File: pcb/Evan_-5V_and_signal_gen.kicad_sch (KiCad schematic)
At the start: 34 parts, among them IC1 TL7660IDGKR, IC2 TL081IDT, IC4 UA78M33CDCYG3, IC9 TL081IDT, J2 ESQ-126-39-L-D, J3 ESQ-126-39-L-D, U5 TPS2069CDBVR_MOSFET

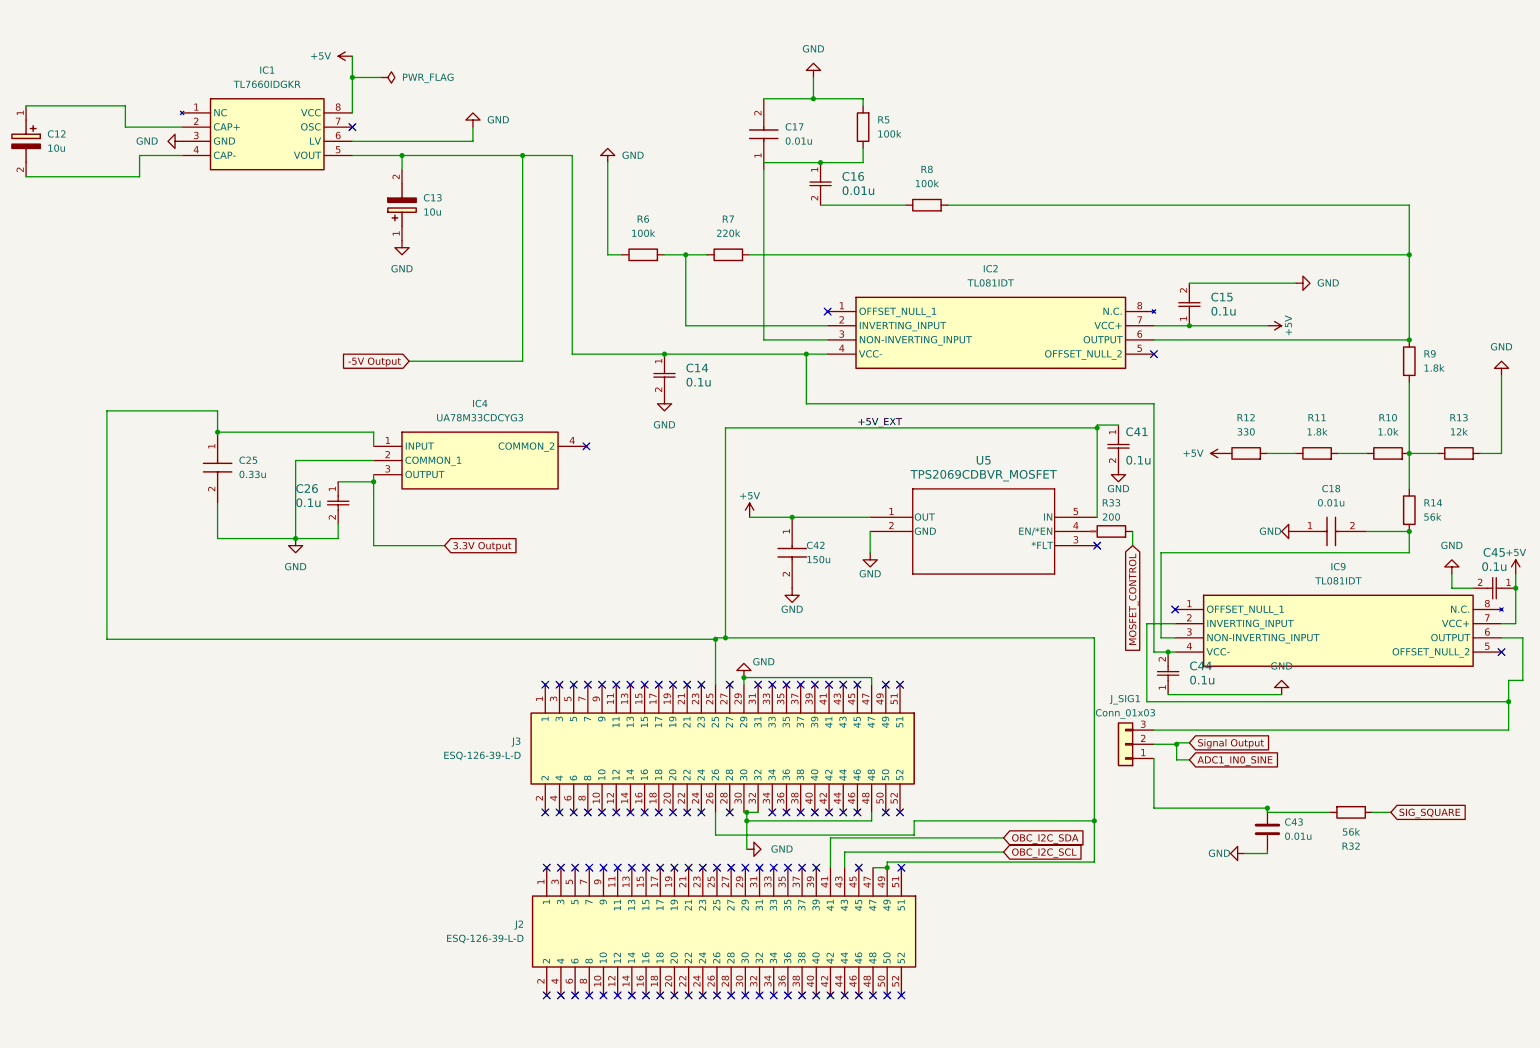
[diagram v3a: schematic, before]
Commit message: clean evan schematic (#22)
* clean evan schematic

* update schematic pdf
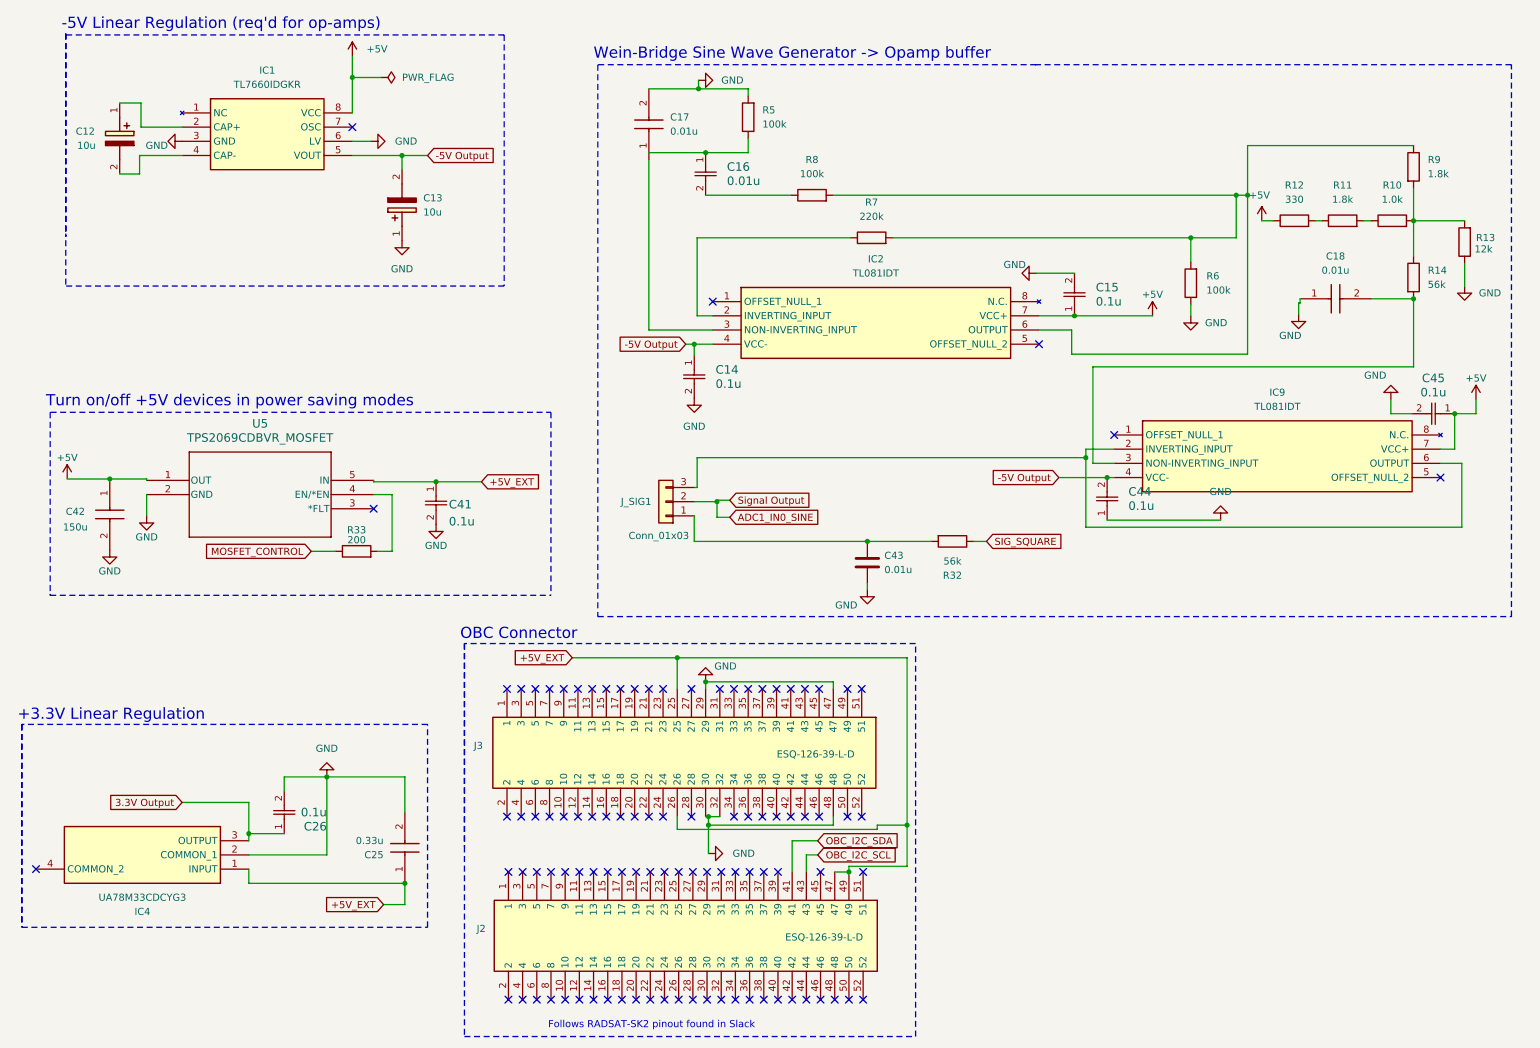
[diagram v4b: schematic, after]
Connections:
- net GND: now also R13.1; no longer R13.2
- net MOSFET_CONTROL: now also R33.1; no longer R33.2
- net at IC2.2 (INVERTING_INPUT), R7.1: no longer R6.2
- net at IC2.6 (OUTPUT), R7.2, R8.2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: now also R6.2
- net at U5.4 (EN/*EN): now also R33.2; no longer R33.1
- net at R10.2, R14.1, R9.2: now also R13.2; no longer R13.1
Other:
- note added: "+3.3V Linear Regulation"
- note added: "-5V Linear Regulation (req'd for op-amps)"
- note added: "Follows RADSAT-SK2 pinout found in Slack"
- note added: "OBC Connector"
- note added: "Turn on/off +5V devices in power saving modes"
- note added: "Wein-Bridge Sine Wave Generator -> Opamp buffer"
- moved on the sheet: C12, C14, C15, C16, C17, C18, C25, C26, C41, C42, C43, C44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
